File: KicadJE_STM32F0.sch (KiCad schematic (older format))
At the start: 66 parts

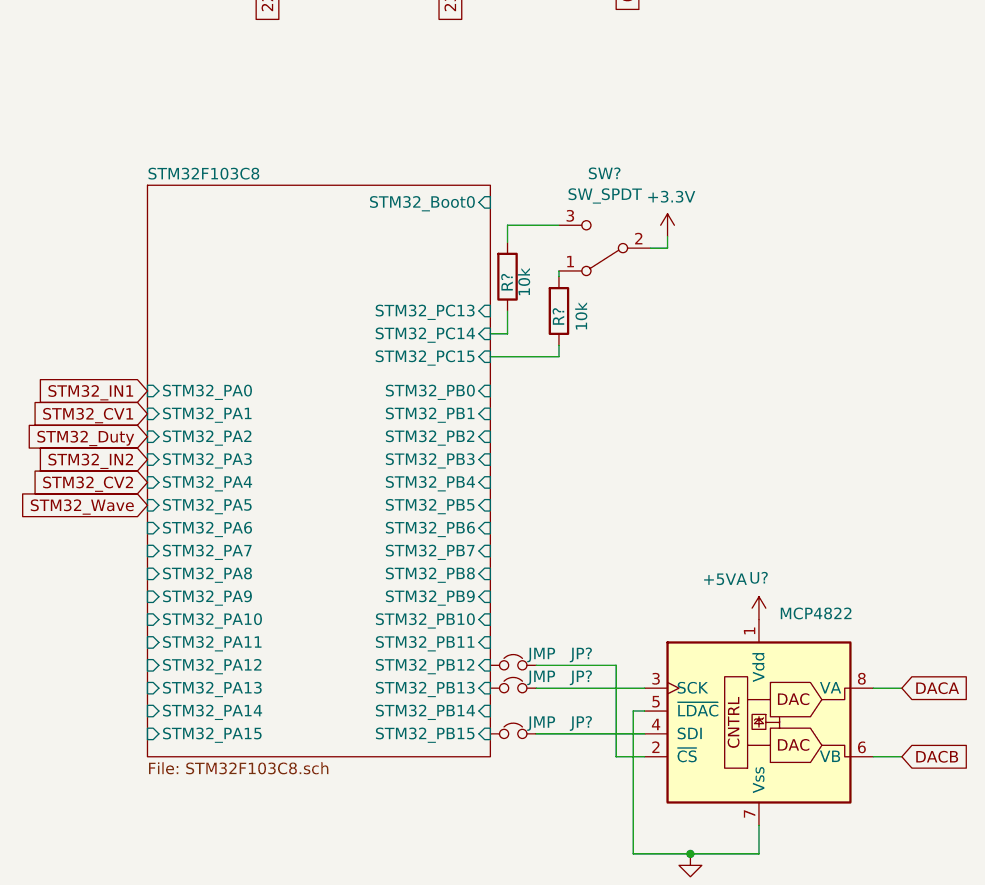
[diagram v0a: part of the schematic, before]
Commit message: STM32 Pin names for serial and USB
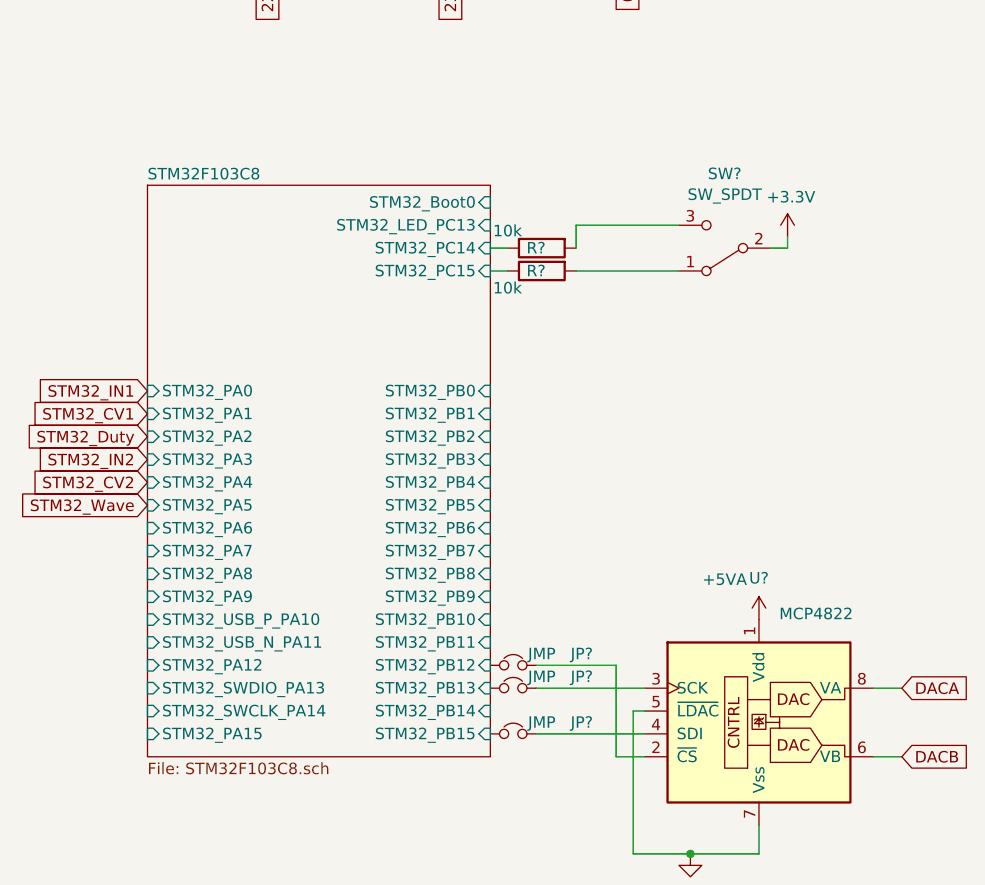
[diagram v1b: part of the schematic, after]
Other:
- moved on the sheet: R?, SW?
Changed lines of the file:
@@
 L Switch:SW_SPDT SW?
 U 1 1 5CE93C75
-P 6000 3000
+P 6525 3000
 AR Path="/5CE3E7A9/5CE93C75" Ref="SW?"  Part="1"
 AR Path="/5CE53731/5CE93C75" Ref="SW?"  Part="1"
-F 0 "SW?" H 6000 2675 50  0000 C CNN
-F 1 "SW_SPDT" H 6000 2766 50  0000 C CNN
-F 2 "" H 6000 3000 50  0001 C CNN
-F 3 "~" H 6000 3000 50  0001 C CNN
-	1    6000 3000
+F 0 "SW?" H 6525 2675 50  0000 C CNN
+F 1 "SW_SPDT" H 6525 2766 50  0000 C CNN
+F 2 "" H 6525 3000 50  0001 C CNN
+F 3 "~" H 6525 3000 50  0001 C CNN
+	1    6525 3000
 	-1   0    0    1
 $EndComp
@@
 F26 "STM32_PA8" I L 4000 4425 50
 F27 "STM32_PA9" I L 4000 4525 50
-F28 "STM32_PA10" I L 4000 4625 50
-F29 "STM32_PA11" I L 4000 4725 50
-F30 "STM32_PA12" I L 4000 4825 50
-F31 "STM32_PA13" I L 4000 4925 50
-F32 "STM32_PA14" I L 4000 5025 50
-F33 "STM32_PA15" I L 4000 5125 50
-F34 "STM32_PC13" I R 5500 3275 50
-F35 "STM32_PC14" I R 5500 3375 50
-F36 "STM32_PC15" I R 5500 3475 50
-F37 "STM32_Boot0" I R 5500 2800 50
+F28 "STM32_PA12" I L 4000 4825 50
+F29 "STM32_PA15" I L 4000 5125 50
+F30 "STM32_PC14" I R 5500 3000 50
+F31 "STM32_PC15" I R 5500 3100 50
+F32 "STM32_Boot0" I R 5500 2800 50
+F33 "STM32_USB_P_PA10" I L 4000 4625 50
+F34 "STM32_USB_N_PA11" I L 4000 4725 50
+F35 "STM32_SWDIO_PA13" I L 4000 4925 50
+F36 "STM32_SWCLK_PA14" I L 4000 5025 50
+F37 "STM32_LED_PC13" I R 5500 2900 50
 $EndSheet
 Wire Wire Line
@@
 	5700 5125 6175 5125
 Wire Wire Line
-	5500 3375 5575 3375
-Wire Wire Line
-	5575 3375 5575 3275
-Wire Wire Line
-	5575 2900 5800 2900
-Wire Wire Line
-	5500 3475 5800 3475
-Wire Wire Line
-	5800 3475 5800 3425
+	5500 3000 5575 3000
 $Comp
 L Device:R R?
 U 1 1 5D0202E9
-P 5800 3275
+P 5725 3100
 AR Path="/5D0202E9" Ref="R?"  Part="1"
 AR Path="/5CD3F059/5D0202E9" Ref="R?"  Part="1"
 AR Path="/5CE53731/5D0202E9" Ref="R?"  Part="1"
-F 0 "R?" V 5800 3300 50  0000 C CNN
-F 1 "10k" V 5900 3300 50  0000 C CNN
-F 2 "Resistor_SMD:R_0805_2012Metric_Pad1.15x1.40mm_HandSolder" V 5730 3275 50  0001 C CNN
-F 3 "~" H 5800 3275 50  0001 C CNN
-	1    5800 3275
-	1    0    0    1
-$EndComp
-Wire Wire Line
-	5800 3125 5800 3100
+F 0 "R?" V 5725 3125 50  0000 C CNN
+F 1 "10k" V 5800 3250 50  0000 C CNN
+F 2 "Resistor_SMD:R_0805_2012Metric_Pad1.15x1.40mm_HandSolder" V 5655 3100 50  0001 C CNN
+F 3 "~" H 5725 3100 50  0001 C CNN
+	1    5725 3100
+	0    -1   1    0
+$EndComp
 $Comp
 L Device:R R?
 U 1 1 5D020B16
-P 5575 3125
+P 5725 3000
 AR Path="/5D020B16" Ref="R?"  Part="1"
 AR Path="/5CD3F059/5D020B16" Ref="R?"  Part="1"
 AR Path="/5CE53731/5D020B16" Ref="R?"  Part="1"
-F 0 "R?" V 5575 3150 50  0000 C CNN
+F 0 "R?" V 5725 3025 50  0000 C CNN
 F 1 "10k" V 5650 3150 50  0000 C CNN
-F 2 "Resistor_SMD:R_0805_2012Metric_Pad1.15x1.40mm_HandSolder" V 5505 3125 50  0001 C CNN
-F 3 "~" H 5575 3125 50  0001 C CNN
-	1    5575 3125
-	1    0    0    1
-$EndComp
-Wire Wire Line
-	5575 2975 5575 2900
+F 2 "Resistor_SMD:R_0805_2012Metric_Pad1.15x1.40mm_HandSolder" V 5655 3000 50  0001 C CNN
+F 3 "~" H 5725 3000 50  0001 C CNN
+	1    5725 3000
+	0    -1   1    0
+$EndComp
 Text GLabel 4000 4125 0    50   Input ~ 0
 STM32_Wave
@@
 L power:+3.3V #PWR?
 U 1 1 5D06D75B
-P 6275 2950
+P 6800 2950
 AR Path="/5CE53731/5CEC50C7/5D06D75B" Ref="#PWR?"  Part="1"
 AR Path="/5CE53731/5D06D75B" Ref="#PWR?"  Part="1"
-F 0 "#PWR?" H 6275 2800 50  0001 C CNN
-F 1 "+3.3V" H 6290 3123 50  0000 C CNN
-F 2 "" H 6275 2950 50  0001 C CNN
-F 3 "" H 6275 2950 50  0001 C CNN
-	1    6275 2950
-	1    0    0    -1
-$EndComp
-Wire Wire Line
-	6200 3000 6275 3000
-Wire Wire Line
-	6275 3000 6275 2950
+F 0 "#PWR?" H 6800 2800 50  0001 C CNN
+F 1 "+3.3V" H 6815 3123 50  0000 C CNN
+F 2 "" H 6800 2950 50  0001 C CNN
+F 3 "" H 6800 2950 50  0001 C CNN
+	1    6800 2950
+	1    0    0    -1
+$EndComp
+Wire Wire Line
+	6725 3000 6800 3000
+Wire Wire Line
+	6800 3000 6800 2950
 $Comp
 L Device:D D?
@@
 	-1   0    0    -1
 $EndComp
+Wire Wire Line
+	5500 3100 5575 3100
+Wire Wire Line
+	5875 3100 6325 3100
+Wire Wire Line
+	5875 3000 5875 2900
+Wire Wire Line
+	5875 2900 6325 2900
 $EndSCHEMATC

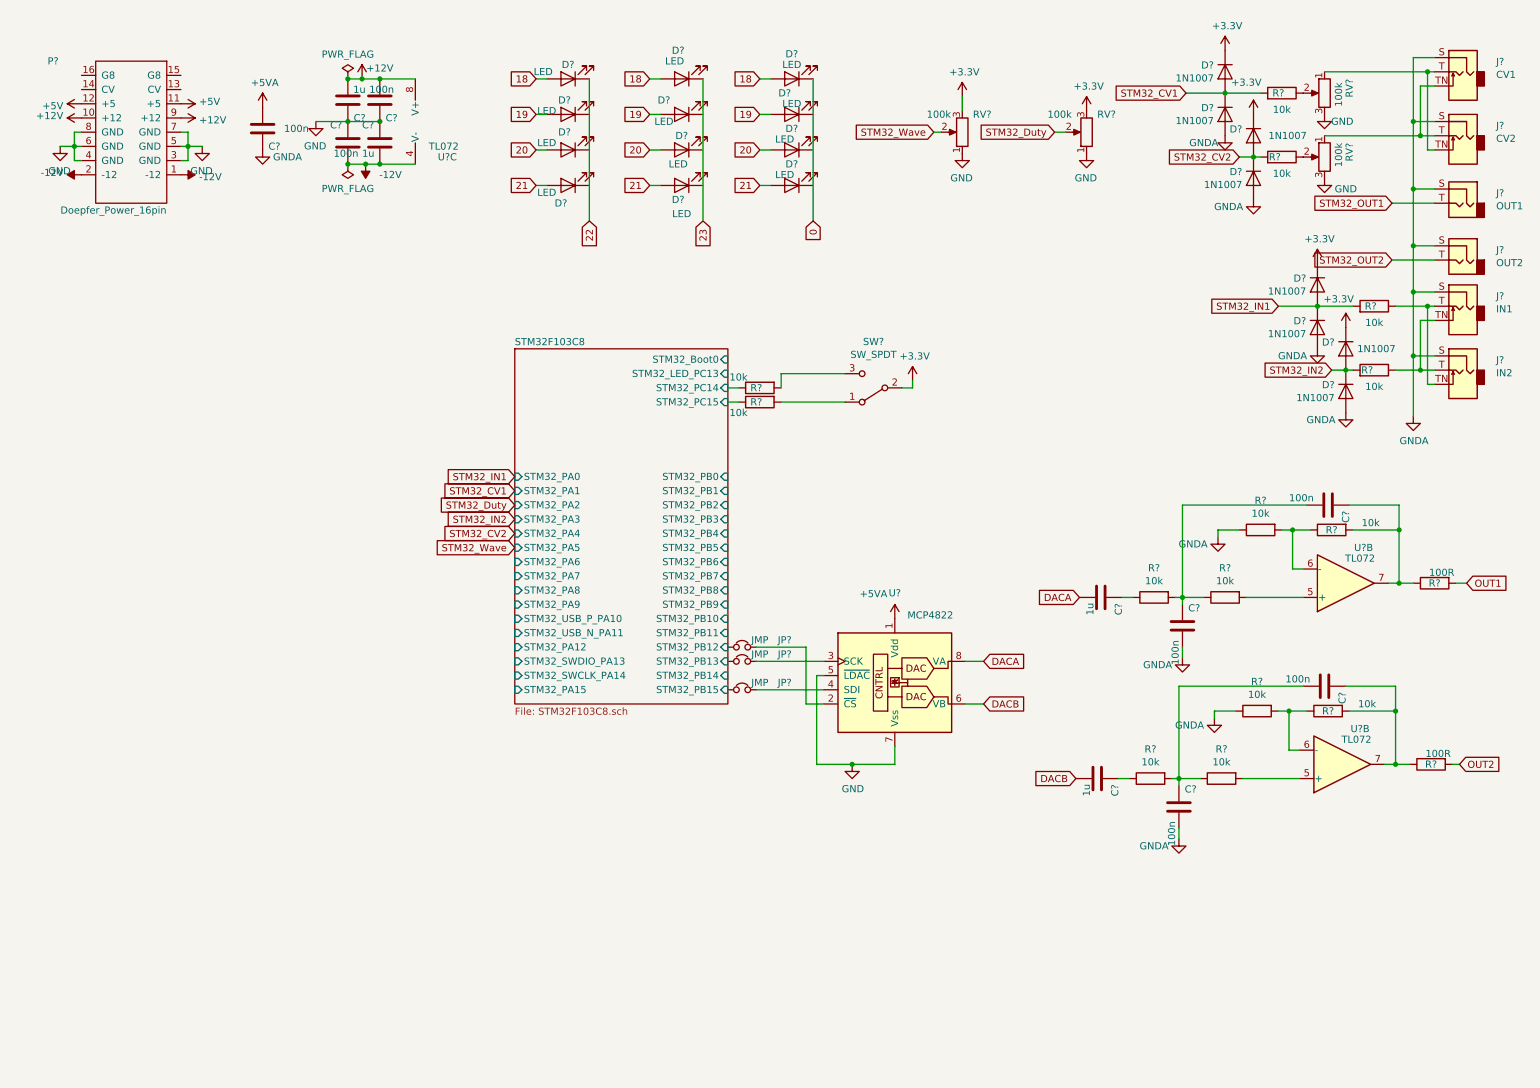
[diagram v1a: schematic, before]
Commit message: Intersheet cleanup
Footprints and cleanup naming on global labels between sheets
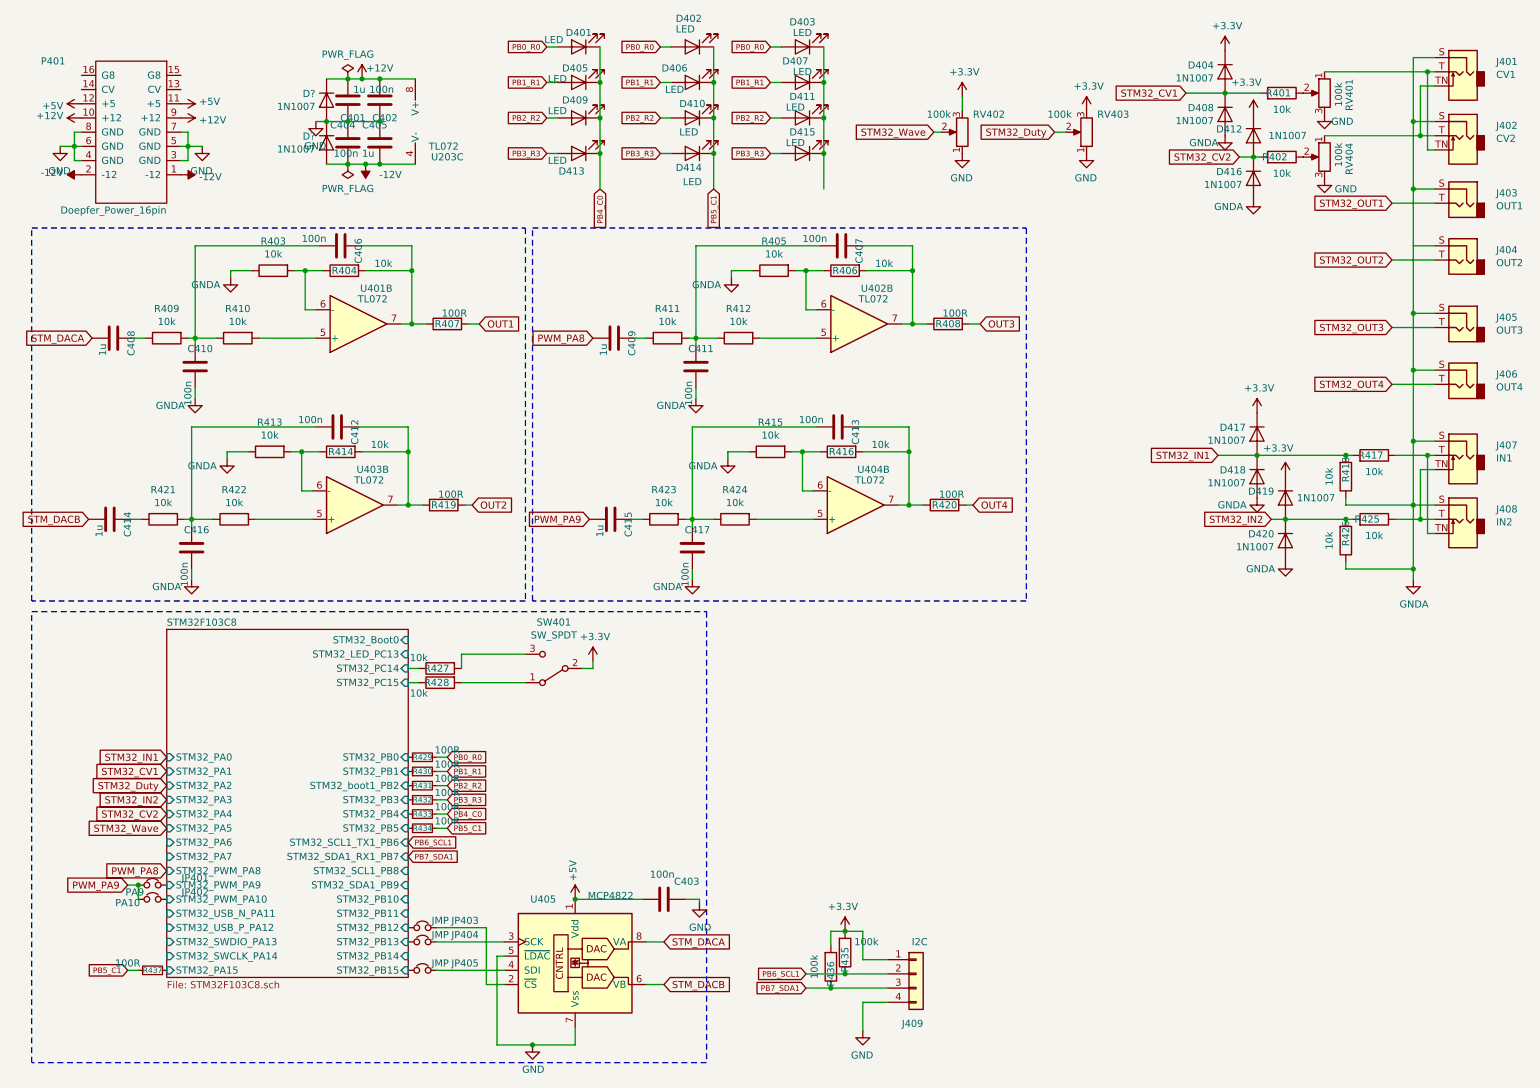
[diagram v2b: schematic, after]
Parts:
- added C407, C411, C413, C417: 100n, Capacitor_SMD:C_0805_2012Metric_Pad1.15x1.40mm_HandSolder, symbol Device:C
- added C409, C415: 1u, Capacitor_SMD:C_1206_3216Metric_Pad1.42x1.75mm_HandSolder, symbol Device:C
- added D? (x2): 1N1007, Diode_SMD:D_SOD-123, symbol Device:D
- added J405: OUT3, AJ-Dropbox-Kicad:PJ301SM, symbol Connector:AudioJack2
- added J406: OUT4, AJ-Dropbox-Kicad:PJ301SM, symbol Connector:AudioJack2
- added J409: I2C, Connector_PinHeader_2.54mm:PinHeader_1x04_P2.54mm_Vertical, symbol Connector_Generic:Conn_01x04
- added JP401: PA9, Jumper:SolderJumper-2_P1.3mm_Bridged_Pad1.0x1.5mm, symbol Device:Jumper_NC_Small
- added JP402: PA10, Jumper:SolderJumper-2_P1.3mm_Open_Pad1.0x1.5mm, symbol Device:Jumper_NC_Small
- added R405, R406, R411, R412, R415, R416, R418, R423, R424, R426: 10k, Resistor_SMD:R_0805_2012Metric_Pad1.15x1.40mm_HandSolder, symbol Device:R
- added R408, R420: 100R, Resistor_SMD:R_0805_2012Metric_Pad1.15x1.40mm_HandSolder, symbol Device:R
- added R429, R430, R431, R432, R433, R434, R437: 100R, Resistor_SMD:R_0805_2012Metric_Pad1.15x1.40mm_HandSolder, symbol Device:R_Small
- added R435, R436: 100k, Resistor_SMD:R_0805_2012Metric_Pad1.15x1.40mm_HandSolder, symbol Device:R
- added U402, U404: TL072, AJ:AJ_SO-8_5.3x6.2mm_P1.27mm, symbol Amplifier_Operational:TL072
- SW401: renamed from SW?; footprint (none) -> AJ:SP1MS1
- U401, U403, U405: renamed from U?; footprint (none) -> AJ:AJ_SO-8_5.3x6.2mm_P1.27mm
- gave numbers to parts that had none: 62
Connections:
- net 0 is gone; now on an unnamed net: D403.1 (K)
- net 22 is gone; now on net PB4_C0: D401.1 (K)
- net 23 is gone; now on net PB5_C1: D402.1 (K)
- net +12V: now also D?.1 (K)
- net +3V3: now also J409.1 (Pin_1), R435.2, R436.2
- net +5V: now also C403.1, U405.1 (Vdd)
- net -12V: now also D?.2 (A)
- net GND: now also C403.2, D?.1 (K), D?.2 (A), J409.4 (Pin_4)
- net GNDA: now also C411.2, C417.2, J405.S, J406.S, R405.1, R415.1, R418.1, R426.1; no longer C403.1
- net STM32F103C8/STM32_PA15: now also R437.1
- net STM32F103C8/STM32_PB0: now also R429.1
- net STM32F103C8/STM32_PB1: now also R430.1
- net STM32F103C8/STM32_PB3: now also R432.1
- net STM32F103C8/STM32_PB4: now also R433.1
- net STM32F103C8/STM32_PB5: now also R434.1
- net STM32_IN1: now also R418.2
- net STM32_IN2: now also R426.2
- net PB4_C0: now reaches D405.1 (K)
- net PB4_C0: now also D409.1 (K), D413.1 (K), R433.2
- net PB5_C1: now reaches D414.1 (K)
- net PB5_C1: now also D406.1 (K), D410.1 (K), R434.2, R437.2
- net at D415.1 (K): now also D407.1 (K), D411.1 (K)
- removed net +5VA: C403.2, U405.1 (Vdd)
- net 18 renamed PB0_R0
- net PB0_R0: now also R429.2
- net 19 renamed PB1_R1
- net PB1_R1: now also R430.2
- net 20 renamed PB2_R2
- net PB2_R2: now also R431.2
- net 21 renamed PB3_R3
- net PB3_R3: now also R432.2
- net DACA renamed STM_DACA
- net DACB renamed STM_DACB
- new net: R424.2, U404.5 (+)
- new net: R415.2, R416.1, U404.6 (-)
- new net: C413.1, R416.2, R420.1, U404.7
- new net: C415.1, R423.1
- new net: C413.2, C417.1, R423.2, R424.1
- new net: R412.2, U402.5 (+)
- new net: R405.2, R406.1, U402.6 (-)
- new net: C407.1, R406.2, R408.1, U402.7
- new net: C409.1, R411.1
- new net: C407.2, C411.1, R411.2, R412.1
- new net OUT3: R408.2
- new net OUT4: R420.2
- new net PB6_SCL1: J409.2 (Pin_2), R435.1
- new net PB7_SDA1: J409.3 (Pin_3), R436.1
- new net PWM_PA8: C409.2
- new net PWM_PA9: C415.2, JP401.2, JP402.2
- new net STM32F103C8/STM32_PWM_PA10: JP402.1
- new net STM32F103C8/STM32_PWM_PA9: JP401.1
- new net STM32F103C8/STM32_boot1_PB2: R431.1
- new net STM32_OUT3: J405.T
- new net STM32_OUT4: J406.T
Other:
- moved on the sheet: C403, C406, C408, C410, C412, C414, C416, D401, D402, D403, D405, D406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

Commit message: LED Matrix ATMega32 rename
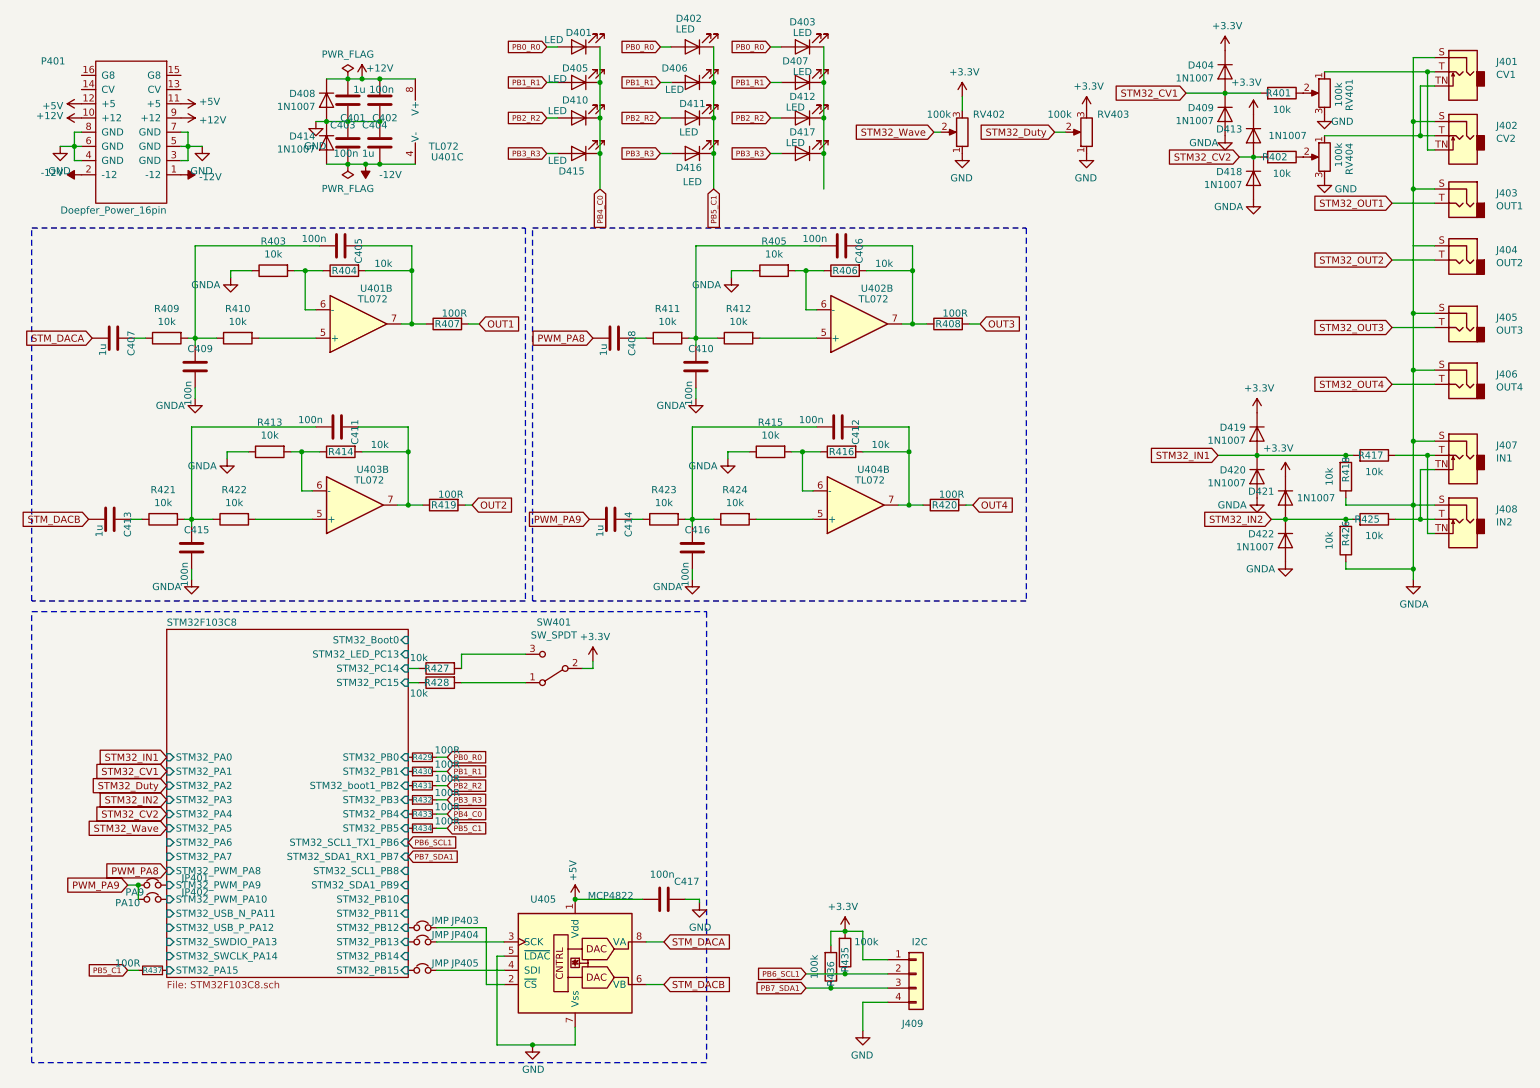
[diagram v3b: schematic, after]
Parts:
- gave numbers to parts that had none: 2
- renumbered C404 to C403, C405 to C404, C406 to C405, C407 to C406, C408 to C407, C409 to C408, C410 to C409, C411 to C410, C412 to C411, C413 to C412, C414 to C413, C415 to C414, C416 to C415, C417 to C416, C403 to C417, D408 to D409, D409 to D410, D410 to D411, D411 to D412, D412 to D413, D413 to D415, D414 to D416, D415 to D417, D416 to D418, D417 to D419, D418 to D420, D419 to D421, D420 to D422, U203 to U401
